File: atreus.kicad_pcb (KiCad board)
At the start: 2 copper layers, 232 x 90 mm, 85 parts

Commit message: changes
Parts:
- removed ?: A-STAR, A_STAR
- removed the D2:2 at (46.3, 31.2)
- removed the D2:2 at (81.8, 48.6)
- removed the D2:2 at (78.5, 67.3)
- removed the D2:2 at (75.2, 86.0)
- removed the D2:2 at (102.8, 39.1)
- removed the D2:2 at (99.5, 57.8)
- removed the D2:2 at (96.2, 76.5)
- removed the D2:2 at (92.9, 95.2)
- removed the D2:2 at (120.6, 47.3)
- removed the D2:2 at (117.3, 66.0)
- removed the D2:2 at (114.0, 84.8)
- removed the D2:2 at (43.0, 49.9)
- removed the D2:2 at (110.7, 103.5)
- removed the D2:2 at (131.0, 97.9)
- removed the D2:2 at (137.2, 97.9)
- removed the D2:2 at (147.6, 47.3)
- removed the D2:2 at (150.9, 66.0)
- removed the D2:2 at (154.2, 84.7)
- removed the D2:2 at (157.5, 103.5)
- removed the D2:2 at (165.4, 39.1)
- removed the D2:2 at (168.7, 57.8)
- removed the D2:2 at (172.0, 76.5)
- removed the D2:2 at (39.7, 68.6)
- removed the D2:2 at (175.3, 95.2)
- removed the D2:2 at (183.1, 29.9)
- removed the D2:2 at (186.4, 48.6)
- removed the D2:2 at (189.7, 67.3)
- removed the D2:2 at (193.0, 86.0)
- removed the D2:2 at (202.7, 31.5)
- removed the D2:2 at (206.0, 50.2)
- removed the D2:2 at (209.3, 68.9)
- removed the D2:2 at (212.6, 87.7)
- removed the D2:2 at (221.9, 31.2)
- removed the D2:2 at (36.4, 87.3)
- removed the D2:2 at (225.2, 49.9)
- removed the D2:2 at (228.5, 68.6)
- removed the D2:2 at (231.8, 87.3)
- removed the D2:2 at (65.6, 31.5)
- removed the D2:2 at (62.3, 50.2)
- removed the D2:2 at (59.0, 68.9)
- removed the D2:2 at (55.7, 87.7)
- removed the D2:2 at (85.1, 29.9)
- removed SW10:0, SW10:1, SW10:2, SW10:3, SW11:0, SW11:1, SW11:2, SW11:3, SW6:0, SW7:0, SW7:1, SW7:2, SW7:3, SW8:0, SW8:1, SW8:2, SW8:3, SW9:0, SW9:1, SW9:2, SW9:3: , MX_FLIP
- added D2:2: , DIODE, F.Cu at (48.0, 28.0)
- added D2:2: , DIODE, F.Cu at (86.0, 39.0)
- added D2:2: , DIODE, F.Cu at (86.0, 58.0)
- added D2:2: , DIODE, F.Cu at (86.0, 77.0)
- added D2:2: , DIODE, F.Cu at (105.0, 26.0)
- added D2:2: , DIODE, F.Cu at (105.0, 45.0)
- added D2:2: , DIODE, F.Cu at (105.0, 64.0)
- added D2:2: , DIODE, F.Cu at (105.0, 83.0)
- added D2:2: , DIODE, F.Cu at (124.0, 31.0)
- added D2:2: , DIODE, F.Cu at (124.0, 50.0)
- added D2:2: , DIODE, F.Cu at (124.0, 69.0)
- added D2:2: , DIODE, F.Cu at (48.0, 47.0)
- added D2:2: , DIODE, F.Cu at (124.0, 88.0)
- added D2:2: , DIODE, F.Cu at (143.0, 79.0)
- added D2:2: , DIODE, F.Cu at (48.0, 66.0)
- added D2:2: , DIODE, F.Cu at (48.0, 85.0)
- added D2:2: , DIODE, F.Cu at (67.0, 25.0)
- added D2:2: , DIODE, F.Cu at (67.0, 44.0)
- added D2:2: , DIODE, F.Cu at (67.0, 63.0)
- added D2:2: , DIODE, F.Cu at (67.0, 82.0)
- added D2:2: , DIODE, F.Cu at (86.0, 20.0)
- moved SW5:0 22.4 mm to (134.0, 79.0), turned to 90 degrees
- moved SW4:3 20.4 mm to (115.0, 88.0), turned to 0 degrees
- moved SW4:2 18.6 mm to (115.0, 69.0), turned to 0 degrees
- moved SW4:1 17.4 mm to (115.0, 50.0), turned to 0 degrees
- moved SW3:3 17.2 mm to (96.0, 83.0), turned to 0 degrees
- moved SW4:0 16.7 mm to (115.0, 31.0), turned to 0 degrees
- moved SW3:2 15.3 mm to (96.0, 64.0), turned to 0 degrees
- moved SW2:3 14.1 mm to (77.0, 77.0), turned to 0 degrees
- moved SW3:1 13.9 mm to (96.0, 45.0), turned to 0 degrees
- moved SW3:0 13.3 mm to (96.0, 26.0), turned to 0 degrees
- moved SW1:3 12.7 mm to (58.0, 82.0), turned to 0 degrees
- moved SW2:2 11.9 mm to (77.0, 58.0), turned to 0 degrees
- moved SW0:3 11.8 mm to (39.0, 85.0), turned to 0 degrees
- moved SW2:1 10.5 mm to (77.0, 39.0), turned to 0 degrees
- moved SW1:2 10.0 mm to (58.0, 63.0), turned to 0 degrees
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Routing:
- net N-row-3: track 299.5 -> 0.00 mm
- net N-row-2: track 281.8 -> 0.00 mm
- net N-row-0: track 264.8 -> 0.00 mm
- net N-row-1: track 226.9 -> 0.00 mm
- net N-col-0: track 218.7 -> 0.00 mm, vias 1 -> 0
- net N-col-10: track 211.5 -> 0.00 mm, vias 1 -> 0
- net N-col-1: track 197.0 -> 0.00 mm, vias 1 -> 0
- net N-col-9: track 193.0 -> 0.00 mm, vias 1 -> 0
- net N-col-2: track 189.2 -> 0.00 mm
- net N-col-8: track 176.2 -> 0.00 mm
- net N-col-3: track 162.6 -> 0.00 mm
- net N-col-7: track 153.6 -> 0.00 mm
- net N-col-6: track 124.5 -> 0.00 mm
- net N-col-4: track 124.1 -> 0.00 mm
- net N-col-5: track 80.4 -> 0.00 mm
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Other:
- board outline removed

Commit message: left hand init
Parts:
- removed the D2:2 at (143.0, 79.0)
- removed the D2:2 at (67.0, 63.0)
- added D2:2: , DIODE, F.Cu at (143.0, 79.0)
- added D2:2: , DIODE, F.Cu at (67.0, 63.0)
- added REF**: Pin_Header_Straight_1x14, Pin_Headers:Pin_Header_Straight_1x14, F.Cu at (144.8, 33.0)
- added REF**: Pin_Header_Straight_1x04, Pin_Headers:Pin_Header_Straight_1x04, F.Cu at (149.9, 58.4)
- added REF**11: Pin_Header_Straight_1x14, Pin_Headers:Pin_Header_Straight_1x14, F.Cu at (129.5, 33.0)
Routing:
- net N-col-2: track 0.00 -> 70.8 mm
- net N-col-3: track 0.00 -> 70.8 mm
- net N-col-0: track 0.00 -> 64.8 mm
- net N-col-1: track 0.00 -> 61.6 mm
- net N-col-4: track 0.00 -> 58.6 mm
- net (no net): track 0.00 -> 20.3 mm
- net N-diode-0: track 0.00 -> 8.78 mm
- net N-diode-20: track 0.00 -> 3.07 mm
- net N-col-5: track 0.00 -> 3.07 mm
- net N-diode-4: track 0.00 -> 3.07 mm
- net N-diode-1: track 0.00 -> 3.07 mm
- net N-diode-8: track 0.00 -> 3.07 mm
- net N-diode-16: track 0.00 -> 3.07 mm
- net N-diode-12: track 0.00 -> 3.07 mm
- net N-diode-9: track 0.00 -> 3.07 mm
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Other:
- board outline added: 139.7 x 101.6 mm
- net class Default: clearance 0.254 -> 0.8; trace_width 0.2032 -> 0.5
- rule trace_clearance: 0.254 -> 0.8

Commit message: routing
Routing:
- net N-row-2: track 0.00 -> 113.8 mm
- net N-row-3: track 0.00 -> 83.9 mm
- net N-row-1: track 0.00 -> 83.9 mm
- net N-row-0: track 0.00 -> 83.9 mm
- net N-col-4: track 58.6 -> 70.8 mm
- net N-diode-20: track 3.07 -> 15.2 mm
- net N-diode-6: track 0.00 -> 8.78 mm
- net N-diode-5: track 0.00 -> 8.78 mm
- net N-diode-2: track 0.00 -> 8.78 mm
- net N-diode-7: track 0.00 -> 8.78 mm
- net N-diode-3: track 0.00 -> 8.78 mm
- net N-diode-19: track 0.00 -> 8.78 mm
- net N-diode-9: track 3.07 -> 8.78 mm
- net N-diode-17: track 3.07 -> 8.78 mm
- net N-diode-14: track 3.07 -> 8.78 mm
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
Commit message: routing
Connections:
- REF**11 pad 1: (no net) -> N-col-4
- REF**11 pad 2: (no net) -> N-col-3
- REF**11 pad 3: (no net) -> N-col-2
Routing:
- net N-col-2: track 70.8 -> 150.6 mm
- net N-col-3: track 70.8 -> 126.1 mm
- net N-col-4: track 70.8 -> 96.0 mm
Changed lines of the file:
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@@
     (thickness 1.6002)
     (drawings 7)
-    (tracks 226)
+    (tracks 246)
     (zones 0)
     (modules 45)
@@
     (mod_text_size 1.524 1.524)
     (mod_text_width 0.3048)
-    (pad_size 2.651 1.651)
-    (pad_drill 0.9906)
+    (pad_size 3.032 1.7272)
+    (pad_drill 1.016)
     (pad_to_mask_clearance 0.254)
     (aux_axis_origin 0 0)
@@
     (fp_line (start -3.81 0) (end -1.6637 0) (layer Front) (width 0.6096))
     (fp_line (start 1.6637 0) (end 3.81 0) (layer Front) (width 0.6096))
-    (pad 1 thru_hole circle (at -3.81 0 180) (size 1.651 1.651) (drill 0.9906) (layers *.Cu *.SilkS *.Mask)
+    (pad 1 thru_hole oval (at -3.81 0 180) (size 1.651 5) (drill 0.9906) (layers *.Cu *.SilkS *.Mask)
       (net 1 N-row-0))
-    (pad 2 thru_hole rect (at 3.81 0) (size 1.651 1.651) (drill 0.9906) (layers *.Cu *.SilkS *.Mask)
+    (pad 2 thru_hole rect (at 3.81 0) (size 2.651 1.651) (drill 0.9906) (layers *.Cu *.SilkS *.Mask)
       (net 11 N-diode-0))
     (pad 99 smd rect (at -1.6637 0) (size 0.8382 0.8382) (layers Front F.Paste F.Mask))
@@
     (fp_line (start -1.55 0) (end -1.55 -1.55) (layer F.SilkS) (width 0.15))
     (fp_line (start -1.55 -1.55) (end 1.55 -1.55) (layer F.SilkS) (width 0.15))
-    (pad 1 thru_hole rect (at 0 0) (size 3.032 1.7272) (drill 1.016) (layers *.Cu *.Mask F.SilkS))
-    (pad 2 thru_hole oval (at 0 2.54) (size 3.032 1.7272) (drill 1.016) (layers *.Cu *.Mask F.SilkS))
-    (pad 3 thru_hole oval (at 0 5.08) (size 3.032 1.7272) (drill 1.016) (layers *.Cu *.Mask F.SilkS))
+    (pad 1 thru_hole rect (at 0 0) (size 3.032 1.7272) (drill 1.016) (layers *.Cu *.Mask F.SilkS)
+      (net 9 N-col-4))
+    (pad 2 thru_hole oval (at 0 2.54) (size 3.032 1.7272) (drill 1.016) (layers *.Cu *.Mask F.SilkS)
+      (net 8 N-col-3))
+    (pad 3 thru_hole oval (at 0 5.08) (size 3.032 1.7272) (drill 1.016) (layers *.Cu *.Mask F.SilkS)
+      (net 7 N-col-2))
     (pad 4 thru_hole oval (at 0 7.62) (size 3.032 1.7272) (drill 1.016) (layers *.Cu *.Mask F.SilkS))
     (pad 5 thru_hole oval (at 0 10.16) (size 3.032 1.7272) (drill 1.016) (layers *.Cu *.Mask F.SilkS))
@@
   (segment (start 55.46 19.92) (end 55.46 21.19) (width 0.5) (layer Front) (net 6))
   (segment (start 55.46 21.19) (end 54.19 22.46) (width 0.5) (layer Front) (net 6))
+  (segment (start 132.715 38.1) (end 129.54 38.1) (width 0.5) (layer Front) (net 7))
+  (segment (start 134.01501 36.79999) (end 132.715 38.1) (width 0.5) (layer Front) (net 7))
+  (segment (start 92.71 15.875) (end 120.516982 15.875) (width 0.5) (layer Front) (net 7))
+  (segment (start 120.516982 15.875) (end 134.01501 29.373028) (width 0.5) (layer Front) (net 7))
+  (segment (start 134.01501 29.373028) (end 134.01501 36.79999) (width 0.5) (layer Front) (net 7))
+  (segment (start 89.561999 12.726999) (end 92.71 15.875) (width 0.5) (layer Front) (net 7))
+  (segment (start 74.46 14.92) (end 76.653001 12.726999) (width 0.5) (layer Front) (net 7))
+  (segment (start 76.653001 12.726999) (end 89.561999 12.726999) (width 0.5) (layer Front) (net 7))
   (segment (start 73.19 55.46) (end 73.19 56.456666) (width 0.5) (layer Front) (net 7))
   (segment (start 73.19 56.456666) (end 73.820901 57.087567) (width 0.5) (layer Front) (net 7))
@@
   (segment (start 73.820901 34.212653) (end 73.19 34.843554) (width 0.5) (layer Front) (net 7))
   (segment (start 73.19 34.843554) (end 73.19 36.46) (width 0.5) (layer Front) (net 7))
+  (segment (start 132.08 35.56) (end 129.54 35.56) (width 0.5) (layer Front) (net 8))
+  (segment (start 132.715 34.925) (end 132.08 35.56) (width 0.5) (layer Front) (net 8))
+  (segment (start 132.715 29.911509) (end 132.715 34.925) (width 0.5) (layer Front) (net 8))
+  (segment (start 95.653001 18.726999) (end 121.53049 18.726999) (width 0.5) (layer Front) (net 8))
+  (segment (start 121.53049 18.726999) (end 132.715 29.911509) (width 0.5) (layer Front) (net 8))
+  (segment (start 93.46 20.92) (end 95.653001 18.726999) (width 0.5) (layer Front) (net 8))
+  (segment (start 131.556 35.56) (end 129.54 35.56) (width 0.5) (layer Front) (net 8))
   (segment (start 92.19 61.46) (end 92.820901 62.090901) (width 0.5) (layer Front) (net 8))
   (segment (start 92.820901 62.090901) (end 92.820901 78.212653) (width 0.5) (layer Front) (net 8))
@@
   (segment (start 93.46 20.92) (end 93.46 22.19) (width 0.5) (layer Front) (net 8))
   (segment (start 93.46 22.19) (end 92.19 23.46) (width 0.5) (layer Front) (net 8))
+  (segment (start 123.825 22.86) (end 129.54 28.575) (width 0.5) (layer Front) (net 9))
+  (segment (start 129.54 28.575) (end 129.54 31.106399) (width 0.5) (layer Front) (net 9))
+  (segment (start 112.46 25.92) (end 115.52 22.86) (width 0.5) (layer Front) (net 9))
+  (segment (start 115.52 22.86) (end 123.825 22.86) (width 0.5) (layer Front) (net 9))
+  (segment (start 129.54 31.106399) (end 129.54 33.02) (width 0.5) (layer Front) (net 9))
   (segment (start 112.46 25.92) (end 112.46 27.19) (width 0.5) (layer Front) (net 9))
   (segment (start 112.46 27.19) (end 111.19 28.46) (width 0.5) (layer Front) (net 9))

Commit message: routing
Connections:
- REF**11 pad 10: (no net) -> N-row-3
- REF**11 pad 11: (no net) -> N-row-1
- REF**11 pad 13: (no net) -> N-col-5
- REF**11 pad 14: (no net) -> N-row-2
- REF**11 pad 4: (no net) -> N-row-0
- REF**11 pad 8: (no net) -> N-col-0
- REF**11 pad 9: (no net) -> N-col-1
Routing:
- net N-col-0: track 64.8 -> 239.4 mm
- net N-col-1: track 61.6 -> 211.5 mm
- net N-row-3: track 83.9 -> 150.0 mm
- net N-col-5: track 3.07 -> 26.5 mm
- net N-row-2: track 113.8 -> 124.3 mm
- net N-row-0: track 83.9 -> 94.2 mm
- net N-row-1: track 83.9 -> 93.0 mm

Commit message: routing done
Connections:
- REF**11 pad 1: N-col-4 -> N-col-3
- REF**11 pad 2: N-col-3 -> N-col-2
- REF**11 pad 3: N-col-2 -> N-row-0
- REF**11 pad 4: N-row-0 -> N-col-4
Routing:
- net N-col-3: track 126.1 -> 117.4 mm
- net N-col-4: track 96.0 -> 88.6 mm
- net N-row-3: track 150.0 -> 154.7 mm
- net N-col-0: track 239.4 -> 244.1 mm
- net N-col-1: track 211.5 -> 216.2 mm
- net N-row-0: track 94.2 -> 92.1 mm
- net N-col-2: track 150.6 -> 149.6 mm

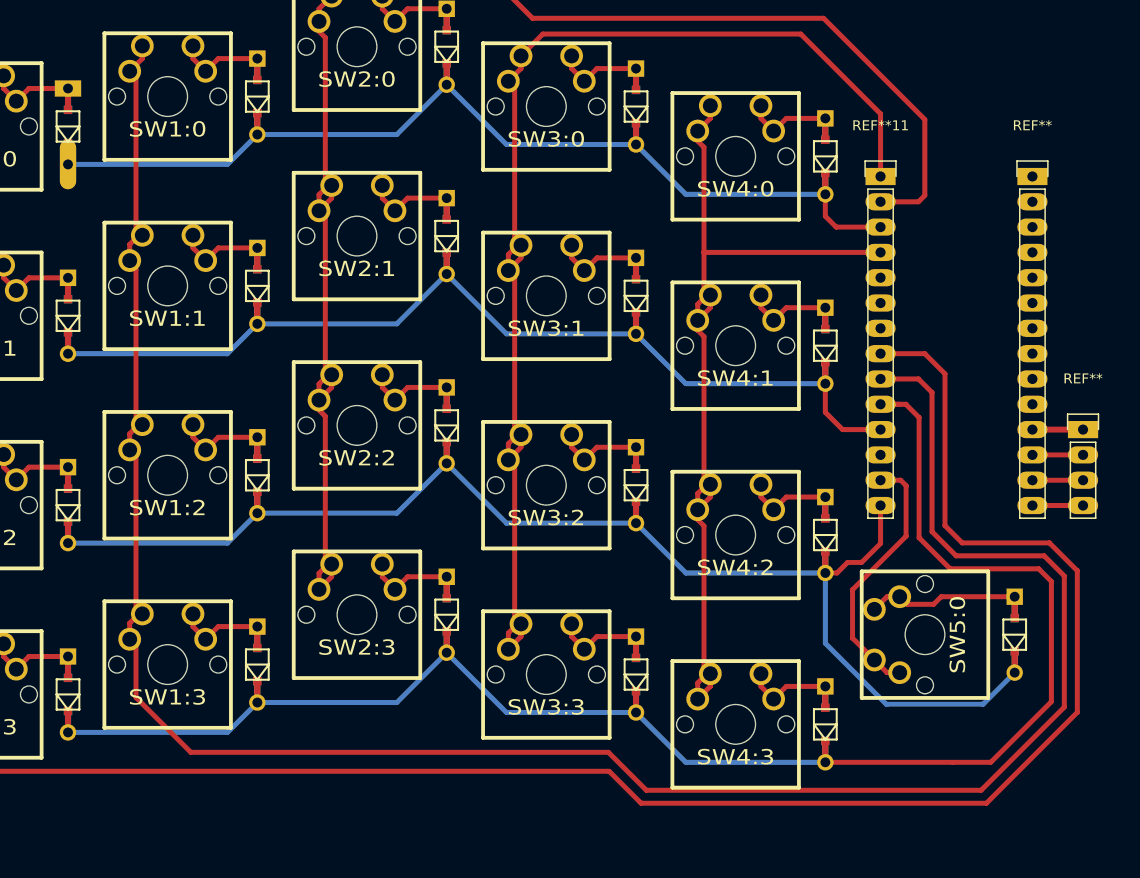
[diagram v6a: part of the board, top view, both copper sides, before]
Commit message: make diode pads bigger
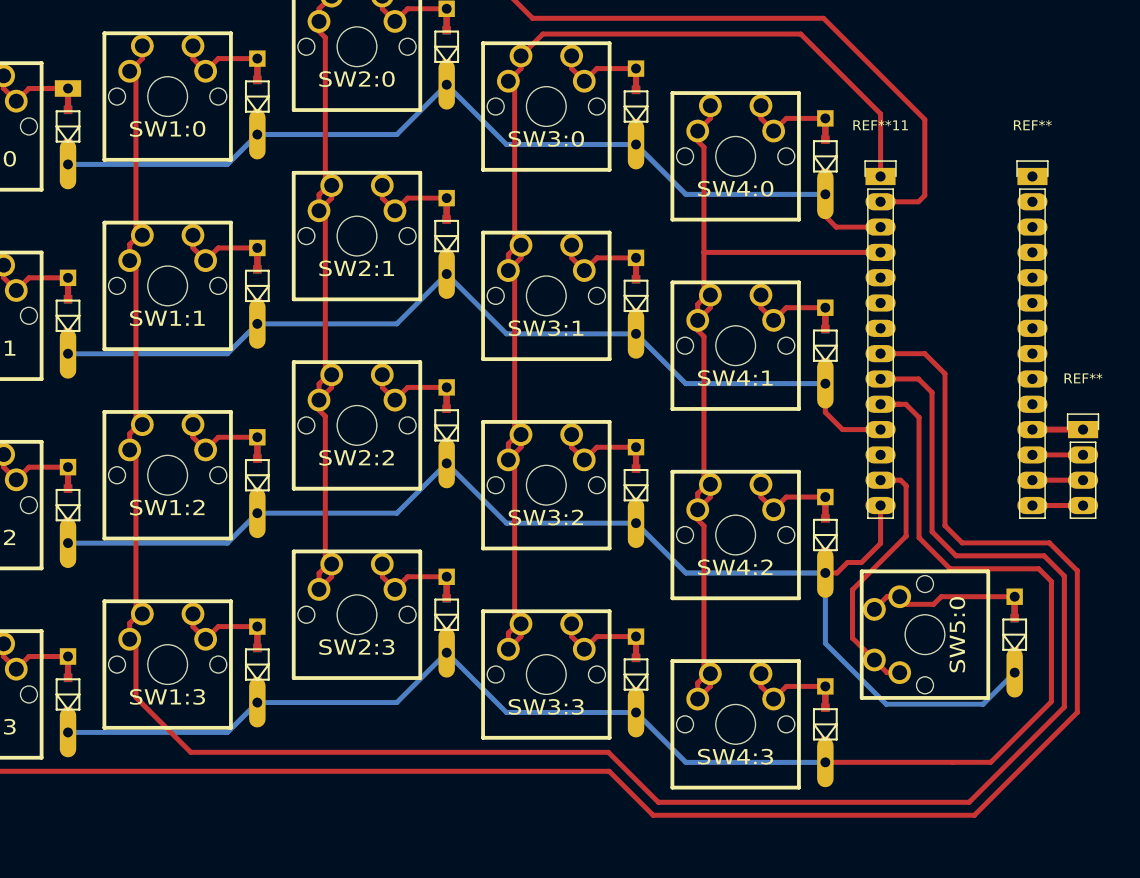
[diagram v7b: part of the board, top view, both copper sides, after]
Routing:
- net N-col-1: track 216.2 -> 217.2 mm
- net N-col-0: track 244.1 -> 245.1 mm
